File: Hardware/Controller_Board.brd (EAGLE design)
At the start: 100 x 100 mm, 28 parts, among them Q7 3.6864MHz, U1 ATMEGA328P-PU, U2 REF3020AIDBZT

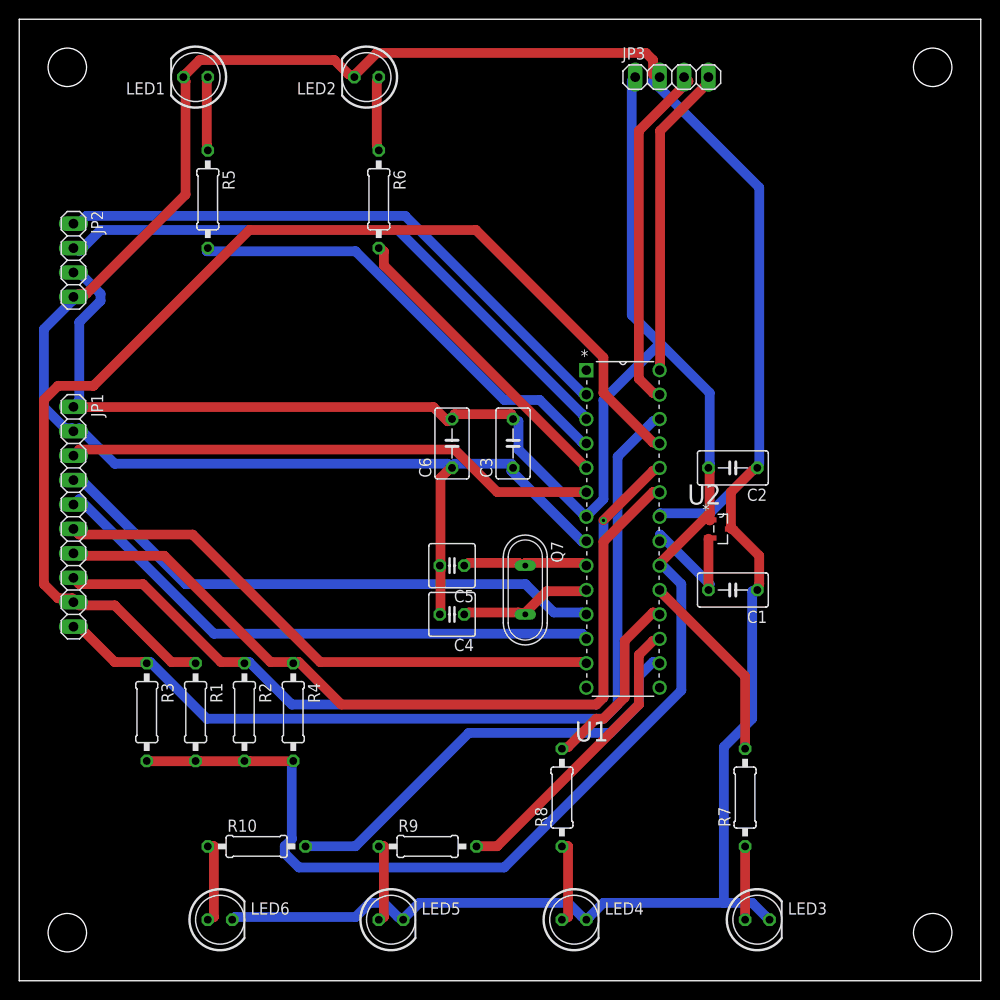
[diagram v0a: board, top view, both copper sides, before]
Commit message: Added microcontroller SPI programming header to the controller board.
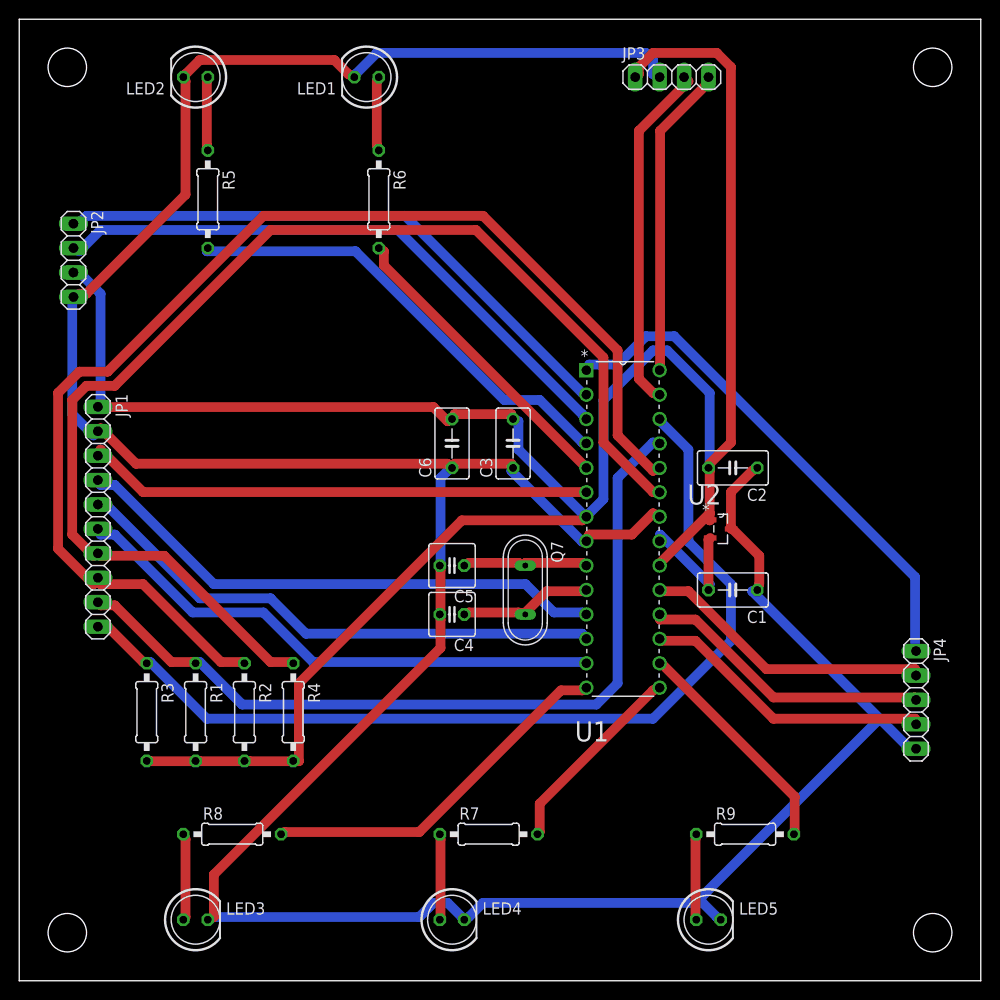
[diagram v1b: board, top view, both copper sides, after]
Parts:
- removed LED6: Led_3, led:LED5MM
- removed R10: 330, resistor:0207/10
- added JP4: Programming, pinhead:1X05
- LED1: value Led_5 -> (none)
- LED2: value Led_4 -> (none)
- LED3: value Led_0 -> (none)
- LED4: value Led_1 -> (none)
- LED5: value Led_2 -> (none)
- moved LED3 58.4 mm to (53.3, 6.35)
- moved R8 34.5 mm to (57.1, 15.2), turned to 0 degrees
- moved R9 33.0 mm to (110.5, 15.2)
- moved LED5 33.0 mm to (106.7, 6.35)
- moved R7 26.9 mm to (83.8, 15.2), turned to 0 degrees
- moved LED1 17.8 mm to (71.1, 94.0)
- moved LED2 17.8 mm to (53.3, 94.0)
- moved LED4 12.7 mm to (80.0, 6.35)
- moved JP1 2.54 mm to (43.2, 48.3)
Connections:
- new net N$21: LED4.A, R7.1
- new net N$28: R9.2, U1.16
- net GND: now also JP4.5; no longer LED6.K
- net N$11: now also LED1.A; no longer LED2.A
- net N$12: now also LED2.A; no longer LED1.A
- net N$15: now also JP4.2, U1.19; no longer LED3.A, R7.1
- net N$17: now also JP4.3, U1.18; no longer LED4.A, R8.1
- net N$18: now also JP4.4, U1.17; no longer R8.2, U1.18
- net N$19: now also JP4.1, U1.1; no longer R7.2, U1.19
- net N$22: now also LED3.A, R8.1; no longer R9.2, U1.17
- net N$24: now also R8.2, U1.14; no longer LED6.A, R10.1
- net N$25: now also R7.2, U1.15; no longer R10.2, U1.16
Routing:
- net N$4: track 86.1 -> 127.6 mm
- net N$3: track 87.4 -> 127.7 mm, vias 1 -> 0
- net N$2: track 121.1 -> 86.7 mm
- net N$19: track 20.2 -> 53.8 mm
- net N$24: track 8.70 -> 38.0 mm
- net N$25: track 46.5 -> 20.7 mm
- net N$28: track 0.00 -> 23.9 mm
- net N$15: track 7.65 -> 30.7 mm
- net N$22: track 31.1 -> 9.02 mm
- net N$17: track 8.70 -> 30.7 mm
- net N$18: track 19.5 -> 30.7 mm
- net N$21: track 0.00 -> 8.91 mm
- net VCC: track 244.9 -> 238.0 mm
- net N$1: track 92.9 -> 99.3 mm
- net N$6: track 59.6 -> 56.6 mm
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
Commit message: Updated controller board PCB with new LDO reference voltage.
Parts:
- added R10, R11: 1K, resistor:0207/10
- C1: value 100n -> 10u Tantalum; device rcl:C050-035X075 -> rcl:E2,5-7
- C2: value 470n -> 10u; device rcl:C050-035X075 -> rcl:E2,5-7
- JP3: value Spare -> I2C temperature sensor
- LED1: value (none) -> Network
- LED2: value (none) -> Status
- LED3: value (none) -> Gas burner
- LED4: value (none) -> Pump
- LED5: value (none) -> Mixing valve
- R1: value 91 1% -> 160 1%
- R3: value 1.3K 1% -> 1K 1%
- R4: value 750 1% -> 470 1%
- U2: value REF3020AIDBZT -> LM1086CT-3.3; device REF3020AIDBZT:SOT95P237X112-3N -> LM1086CT-3.3:TO254P470X1016X2222-3P
- moved U2 20.7 mm to (123.2, 61.0)
- moved C2 16.6 mm to (125.7, 52.1)
- moved C1 13.7 mm to (116.8, 52.1)
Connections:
- removed net N$16: C1.2, U1.21, U2.2
- new net +3V3: C1.+, R1.2, R2.2, R3.2, R4.2, U1.21, U2.2
- net GND: now also C1.-, C2.-, U2.1; no longer C1.1, C2.1, U2.3
- net N$20: now also R11.1
- net N$23: now also R10.1
- net VCC: now also C2.+, R10.2, R11.2, U2.3; no longer C2.2, R1.2, R2.2, R3.2, R4.2, U2.1
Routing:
- net +3V3: track 0.00 -> 117.7 mm
- net VCC: track 238.0 -> 174.5 mm
- net N$4: track 127.6 -> 83.6 mm
- net GND: track 344.7 -> 364.3 mm
- net N$3: track 127.7 -> 112.3 mm
- net N$16: track 14.1 -> 0.00 mm
- net N$2: track 86.7 -> 94.0 mm
- net N$23: track 32.6 -> 35.7 mm
- net N$20: track 36.5 -> 39.4 mm
- net N$14: track 48.1 -> 50.5 mm
- net N$9: track 62.5 -> 64.2 mm
- net N$10: track 61.3 -> 63.0 mm
- net N$1: track 99.3 -> 98.8 mm
- net N$19: track 53.8 -> 54.4 mm
